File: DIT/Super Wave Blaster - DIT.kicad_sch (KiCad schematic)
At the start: 20 parts, among them J1 SPDIF, J4 Power Input, U1 TLV73333PDBV, U2 DIT4096PW, U4 74LVC2G125

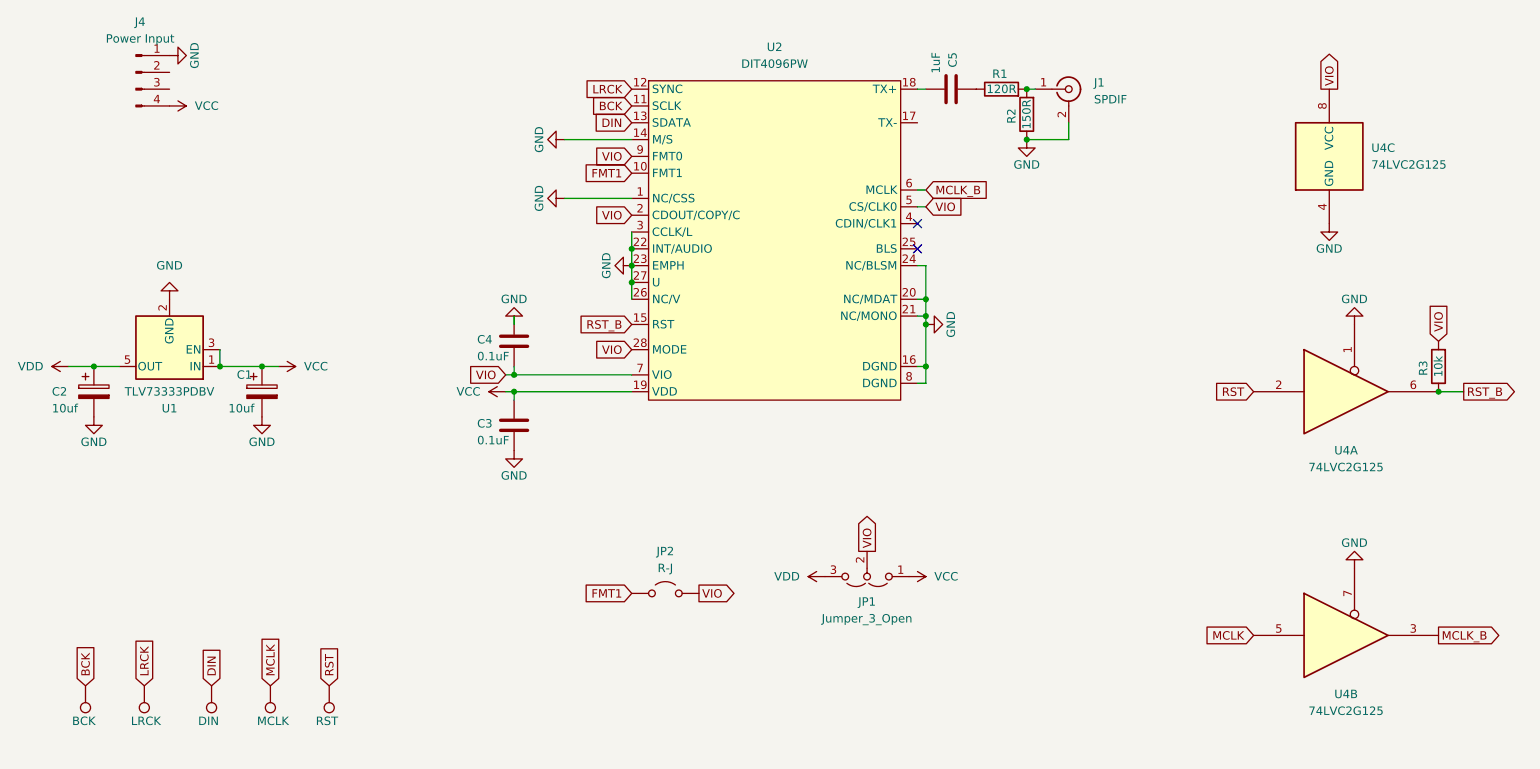
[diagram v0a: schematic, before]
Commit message: DIT v0.2 - compact and right justified only
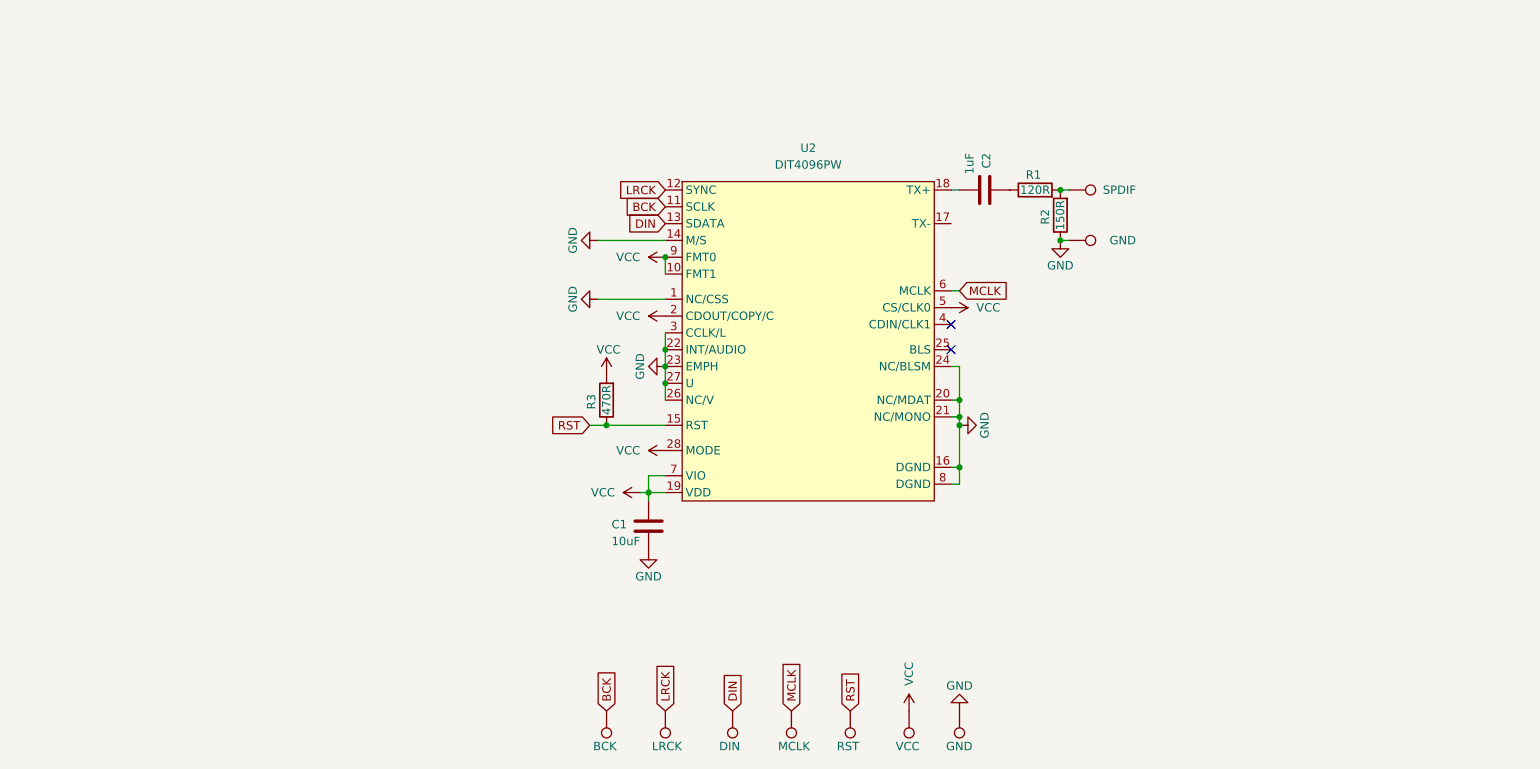
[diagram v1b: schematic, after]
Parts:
- removed C1, C2: 10uf, Capacitor_SMD:C_0805_2012Metric_Pad1.18x1.45mm_HandSolder, symbol Device:C_Polarized
- removed C4: 0.1uF, Capacitor_SMD:C_0805_2012Metric_Pad1.18x1.45mm_HandSolder, symbol Device:C
- removed J1: SPDIF, Connector_Coaxial:U.FL_Hirose_U.FL-R-SMT-1_Vertical, symbol Connector:Conn_Coaxial
- removed J4: Power Input, Connector_PinHeader_2.54mm:PinHeader_1x04_P2.54mm_Vertical, symbol Connector:Conn_01x04_Pin
- removed JP1: Jumper_3_Open, Jumper:SolderJumper-3_P1.3mm_Open_RoundedPad1.0x1.5mm, symbol Jumper:Jumper_3_Open
- removed JP2: R-J, Jumper:SolderJumper-2_P1.3mm_Open_RoundedPad1.0x1.5mm, symbol Jumper:Jumper_2_Open
- removed U1: TLV73333PDBV, Package_TO_SOT_SMD:SOT-23-5, symbol Regulator_Linear:TLV73333PDBV
- removed U4: 74LVC2G125, Package_SO:VSSOP-8_2.3x2mm_P0.5mm, symbol 74xGxx:74LVC2G125
- added TP6: SPDIF, TestPoint:TestPoint_Pad_1.0x1.0mm, symbol Connector:TestPoint
- added TP7, TP9: GND, TestPoint:TestPoint_Pad_1.0x1.0mm, symbol Connector:TestPoint
- added TP8: VCC, TestPoint:TestPoint_Pad_1.0x1.0mm, symbol Connector:TestPoint
- C1: renamed from C3; value 0.1uF -> 10uF
- R3: value 10k -> 470R
- TP1, TP2, TP3, TP4, TP5: footprint TestPoint:TestPoint_Pad_1.5x1.5mm -> TestPoint:TestPoint_Pad_1.0x1.0mm
- U2: footprint Package_SO:SSOP-28_3.9x9.9mm_P0.635mm -> Package_SO:SSOP-28_5.3x10.2mm_P0.65mm
- renumbered C5 to C2
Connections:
- net FMT1 is gone; now on net VCC: U2.10 (FMT1)
- net MCLK_B is gone; now on net MCLK: U2.6 (MCLK)
- net RST_B is gone; now on net RST: R3.1, U2.15 (RST)
- net VIO is gone; now on net VCC: R3.2, U2.2 (CDOUT/COPY/C), U2.28 (MODE), U2.5 (CS/CLK0), U2.7 (VIO), U2.9 (FMT0)
- net GND: now also TP7.1, TP9.1
- net VCC: now also TP8.1
- net at R1.2, R2.2: now also TP6.1
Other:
- moved on the sheet: C1, C2, R1, R2, R3, U2
